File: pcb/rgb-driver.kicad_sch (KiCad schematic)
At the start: 7 parts, among them U8 IS31FL3193

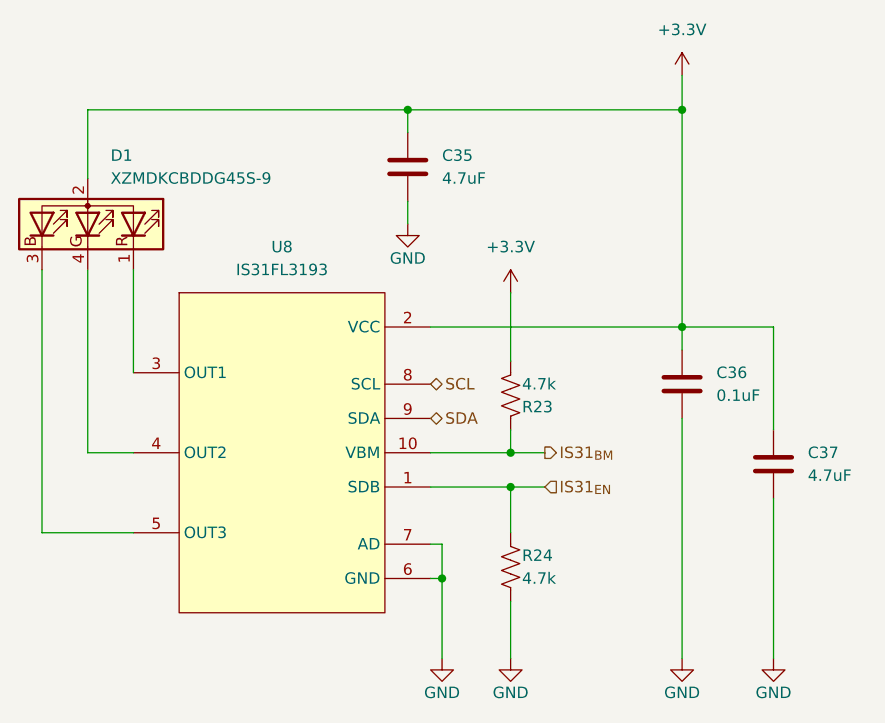
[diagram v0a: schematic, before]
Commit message: Replaced through-hole components with SMD
- Other small edits (e.g. optional jumper to force USB-boot)
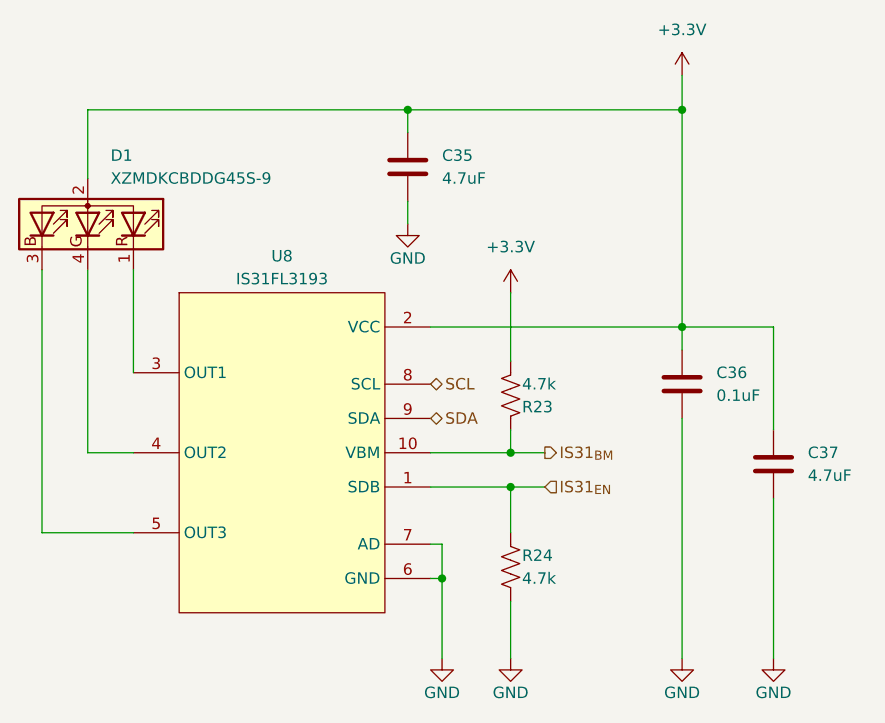
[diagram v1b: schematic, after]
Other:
- company: (none) -> Open Ephys, Inc.
- title: (none) -> Open Ephys Commutator Controller
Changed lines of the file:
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@@
 	(generator_version "8.0")
 	(paper "A5")
+	(title_block
+		(title "Open Ephys Commutator Controller")
+		(rev "D")
+		(company "Open Ephys, Inc.")
+	)
 	(junction
 		(at 106.68 83.82)
@@
 		(on_board yes)
 		(dnp no)
-		(fields_autoplaced yes)
 		(property "Reference" "U8"
-			(at 88.9 46.99 0)
+			(at 88.9 48.006 0)
 			(effects
 				(font
@@
 		)
 		(property "Value" "IS31FL3193"
-			(at 88.9 49.53 0)
-			(effects
-				(font
+			(at 88.9 50.546 0)
+			(effects
+				(font

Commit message: Rev D PCB WIP for Review
- Before going into further minutiae, get review
- Components are laid out and routed
- Fails DRC check, requires vias for better GND plane, there are traces
  in the outer keepout zone, remove S5?
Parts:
- D1: footprint open-ephys:SUNLED_PLCC4-INV_3.2x2.8x1.9mm -> oe:SUNLED_PLCC4-INV_3.2x2.8x1.9mm
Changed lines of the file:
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@@
 			)
 		)
-		(property "Footprint" "open-ephys:SUNLED_PLCC4-INV_3.2x2.8x1.9mm"
+		(property "Footprint" "oe:SUNLED_PLCC4-INV_3.2x2.8x1.9mm"
 			(at 66.04 44.45 0)
 			(effects
